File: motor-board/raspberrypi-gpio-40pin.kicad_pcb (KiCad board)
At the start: 2 copper layers, 81.8 x 38.3 mm, 24 parts, among them J1 Conn_01x15

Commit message: updated bom
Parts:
- F1: footprint footprints:MCCQ-121 -> footprints:MCCQ122
- F2: footprint footprints:littlefuse_448 -> Fuse:Fuse_1206_3216Metric
- J1: value Conn_01x15 -> 1-1734248-5; footprint Connector_FFC-FPC:Molex_502231-1500_1x15-1SH_P0.5mm_Vertical -> footprints:TE_1-1734248-5
- moved F2 24.3 mm to (260.5, 145.2), turned to 90 degrees
- moved R16 9.08 mm to (223.1, 127.9), turned to 0 degrees
- moved F1 8.13 mm to (254.6, 144.4)
- moved J1 7.19 mm to (237.1, 129.4)
- moved C5 4.99 mm to (223.1, 130.9)
- moved SX1 4.07 mm to (229.5, 134.5)
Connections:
- J1 pad 15: Net-(J1-Pad15) -> SPI1_MISO
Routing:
- net +3V3: track 176.5 -> 320.0 mm, vias 0 -> 1
- net GND: track 7.35 -> 140.4 mm
- net SPI1_MOSI: track 5.78 -> 14.9 mm
- net SPI1_CE: track 64.0 -> 73.0 mm
- net ENABLE: track 55.7 -> 64.6 mm
- net +24V: track 6.23 -> 12.2 mm
- net Net-(F1-Pad1): track 26.7 -> 21.7 mm
- net X_STEP: track 13.7 -> 18.1 mm
- net Net-(F2-Pad2): track 15.7 -> 13.1 mm
- net X_DIR: track 15.2 -> 17.0 mm
- net Z_PO: track 64.5 -> 62.8 mm
- net Y_1B: track 9.80 -> 8.75 mm
- net X_PO: track 30.6 -> 31.4 mm
- net Z_2B: track 7.63 -> 7.12 mm

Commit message: new boards
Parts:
- added G1: Logo_Open_Hardware_Small, footprints:hexastorm, F.Cu at (218.2, 147.0)
- H1, H2: footprint MountingHole:MountingHole_2.2mm_M2 -> MountingHole:MountingHole_2.7mm_M2.5
- moved SY1 0.99 mm to (214.4, 134.7)
- moved C19 0.34 mm to (221.5, 159.3)
- moved J1 0.26 mm to (237.0, 129.2), turned to 0 degrees
- moved SZ1 0.13 mm to (195.7, 134.9)
- moved C20 0.13 mm to (200.3, 159.5)
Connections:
- J1 pad 1: ENABLE -> (no net)
- J1 pad 10: Y_PO -> X_DIR
- J1 pad 10_1: Y_PO -> X_DIR
- J1 pad 11: Z_STEP -> X_STEP
- J1 pad 11_1: Z_STEP -> X_STEP
- J1 pad 12: Z_DIR -> SPI1_CE
- J1 pad 12_1: Z_DIR -> SPI1_CE
- J1 pad 13: Z_PO -> SPI1_SCL
- J1 pad 13_1: Z_PO -> SPI1_SCL
- J1 pad 14: SPI1_MISO -> SPI1_MOSI
- J1 pad 14_1: SPI1_MISO -> SPI1_MOSI
- J1 pad 15: SPI1_MISO -> ENABLE
- J1 pad 15_1: SPI1_MISO -> ENABLE
- J1 pad 1_1: ENABLE -> (no net)
- J1 pad 2: SPI1_MOSI -> SPI1_MISO
- J1 pad 2_1: SPI1_MOSI -> SPI1_MISO
- J1 pad 3: SPI1_SCL -> Z_PO
- J1 pad 3_1: SPI1_SCL -> Z_PO
- J1 pad 4: SPI1_CE -> Z_DIR
- J1 pad 4_1: SPI1_CE -> Z_DIR
- J1 pad 5: X_STEP -> Z_STEP
- J1 pad 5_1: X_STEP -> Z_STEP
- J1 pad 6: X_DIR -> Y_PO
- J1 pad 6_1: X_DIR -> Y_PO
- J1 pad 7: X_PO -> Y_DIR
- J1 pad 7_1: X_PO -> Y_DIR
- J1 pad 9: Y_DIR -> X_PO
- J1 pad 9_1: Y_DIR -> X_PO
- MX1 pad 6: Net-(MX1-Pad6) -> (no net)
- MY1 pad 6: Net-(MY1-Pad6) -> (no net)
- MZ1 pad 6: Net-(MZ1-Pad6) -> (no net)
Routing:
- net +3V3: track 320.0 -> 261.1 mm
- net SPI1_MISO: track 56.8 -> 52.0 mm
- net X_STEP: track 18.1 -> 16.4 mm
- net Y_PO: track 40.8 -> 40.0 mm
- net GND: track 140.4 -> 140.9 mm, vias 2 -> 7
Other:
- board text removed: "HEXASTORM"

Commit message: updated bom
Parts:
- moved J1 0.34 mm to (237.1, 129.5), turned to 180 degrees
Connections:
- J1 pad 1: (no net) -> ENABLE
- J1 pad 10: X_DIR -> Y_PO
- J1 pad 10_1: X_DIR -> Y_PO
- J1 pad 11: X_STEP -> Z_STEP
- J1 pad 11_1: X_STEP -> Z_STEP
- J1 pad 12: SPI1_CE -> Z_DIR
- J1 pad 12_1: SPI1_CE -> Z_DIR
- J1 pad 13: SPI1_SCL -> Z_PO
- J1 pad 13_1: SPI1_SCL -> Z_PO
- J1 pad 14: SPI1_MOSI -> SPI1_MISO
- J1 pad 14_1: SPI1_MOSI -> SPI1_MISO
- J1 pad 15: ENABLE -> (no net)
- J1 pad 15_1: ENABLE -> (no net)
- J1 pad 1_1: (no net) -> ENABLE
- J1 pad 2: SPI1_MISO -> SPI1_MOSI
- J1 pad 2_1: SPI1_MISO -> SPI1_MOSI
- J1 pad 3: Z_PO -> SPI1_SCL
- J1 pad 3_1: Z_PO -> SPI1_SCL
- J1 pad 4: Z_DIR -> SPI1_CE
- J1 pad 4_1: Z_DIR -> SPI1_CE
- J1 pad 5: Z_STEP -> X_STEP
- J1 pad 5_1: Z_STEP -> X_STEP
- J1 pad 6: Y_PO -> X_DIR
- J1 pad 6_1: Y_PO -> X_DIR
- J1 pad 7: Y_DIR -> X_PO
- J1 pad 7_1: Y_DIR -> X_PO
- J1 pad 9: X_PO -> Y_DIR
- J1 pad 9_1: X_PO -> Y_DIR
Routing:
- net X_DIR: track 17.0 -> 17.7 mm

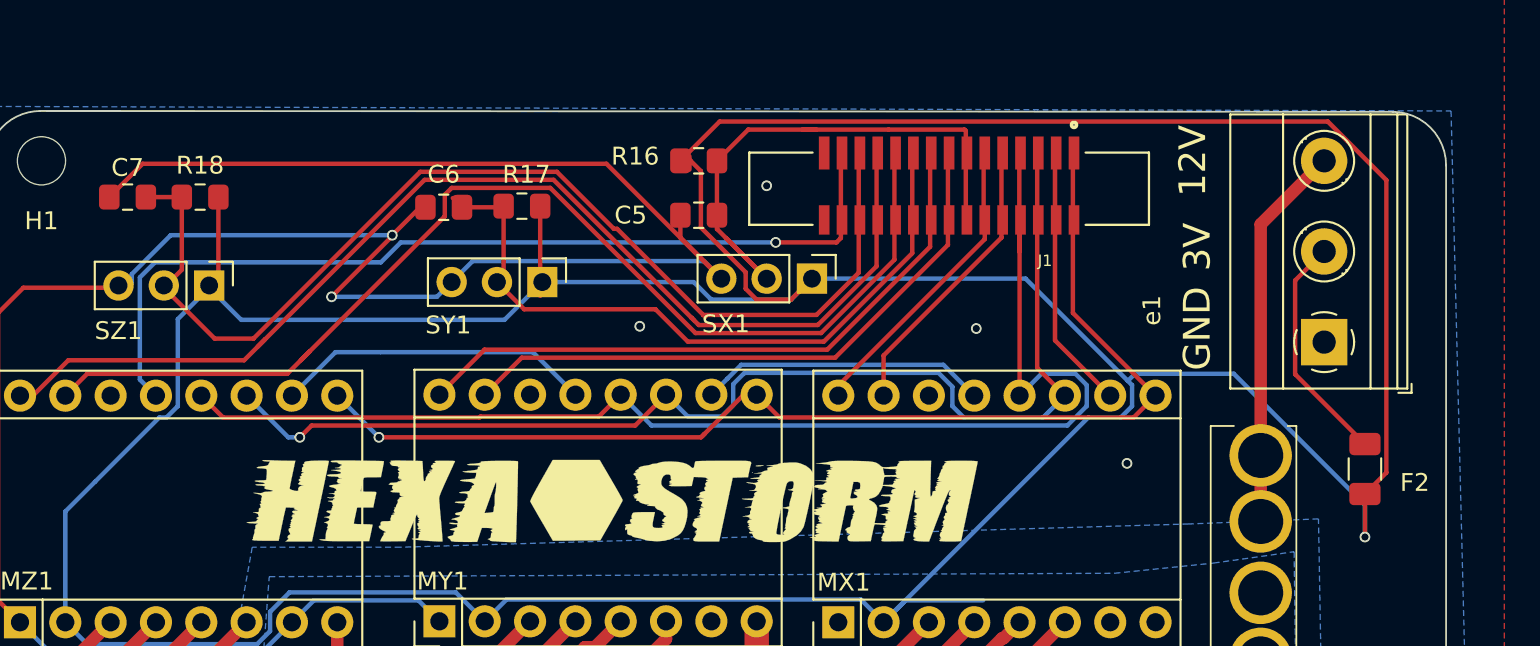
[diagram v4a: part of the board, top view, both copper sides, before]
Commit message: 3V routed via flatex
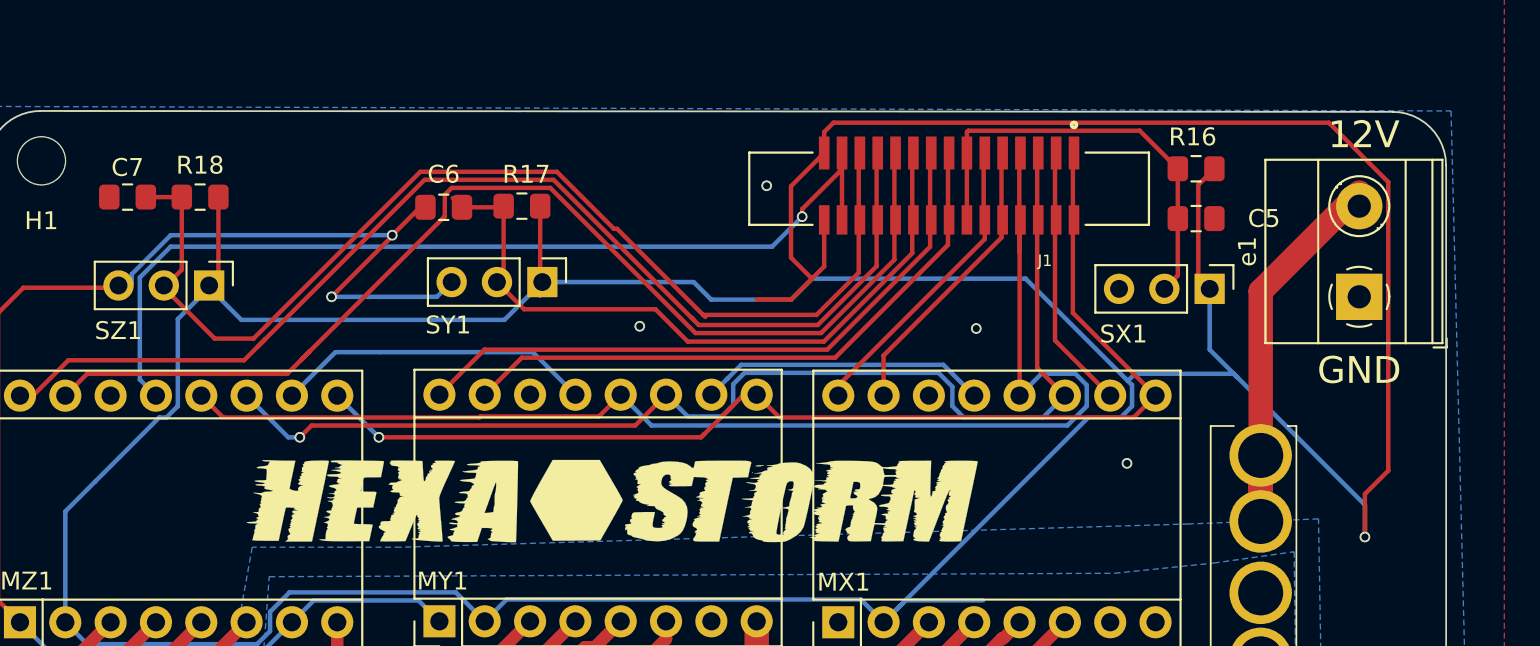
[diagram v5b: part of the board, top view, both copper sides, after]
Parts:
- removed F2: 2A, Fuse:Fuse_1206_3216Metric
- e1: value Screw_Terminal_01x03 -> Screw_Terminal_01x02; footprint TerminalBlock_Phoenix:TerminalBlock_Phoenix_MKDS-1,5-3-5.08_1x03_P5.08mm_Horizontal -> TerminalBlock_Phoenix:TerminalBlock_Phoenix_MKDS-1,5-2-5.08_1x02_P5.08mm_Horizontal
- moved R16 27.9 mm to (251.0, 128.3), turned to 180 degrees
- moved C5 27.9 mm to (251.0, 131.1), turned to 180 degrees
- moved SX1 22.3 mm to (251.8, 135.1)
- moved e1 3.21 mm to (260.1, 135.5)
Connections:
- J1 pad 15: (no net) -> +3V3
- J1 pad 15_1: (no net) -> +3V3
- e1 pad 2: Net-(F2-Pad2) -> Net-(F1-Pad1)
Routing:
- net GND: track 140.9 -> 82.5 mm
- net Net-(F2-Pad2): track 13.1 -> 0.00 mm
- net +3V3: track 261.1 -> 267.7 mm
- net X_PO: track 31.4 -> 24.7 mm
- net Net-(F1-Pad1): track 21.7 -> 26.5 mm
- net SPI1_MISO: track 52.0 -> 53.8 mm
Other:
- board text removed: "3V"
